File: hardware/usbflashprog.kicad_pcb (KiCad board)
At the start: 2 copper layers, 211 x 122 mm, 123 parts, among them J1 12-18V, J2 Parallel Adapter, J3 Serial Adapter, Q1 BC547, Q10 BC557, Q11 BC557, Q12 BC547, Q13 BC547, Q14 BC547, Q15 BC547, Q16 BC547, Q2 BC327, Q3 BC327, Q4 BC327, Q5 TIP120, Q6 BC327, Q7 BC557, Q8 BC557, Q9 BC557, U1 7809, U10 74HC595, U11 74HC165, U12 74HC165, U2 74LS06N, U3 Pico, U4 74HC595, U5 74HC595, U6 74HC595, U7 74HC595, U8 74LS06N, U9 74HC595

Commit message: Rev.E. Updated specifications document and hardware design.
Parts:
- C1, C2, C6: footprint Capacitor_THT:CP_Radial_D8.0mm_P3.50mm -> Capacitor_THT:CP_Radial_D5.0mm_P2.50mm
- C4: footprint Capacitor_THT:CP_Radial_D10.0mm_P7.50mm -> Capacitor_THT:CP_Radial_D8.0mm_P3.80mm
- C8: footprint Capacitor_THT:C_Disc_D6.0mm_W2.5mm_P5.00mm -> Capacitor_THT:CP_Radial_D8.0mm_P3.50mm
- L2: footprint Inductor_THT:L_Toroid_Vertical_L16.0mm_W8.0mm_P7.62mm -> Inductor_THT:L_Toroid_Vertical_L13.0mm_W6.5mm_P5.60mm
- R52: footprint Resistor_THT:R_Axial_DIN0207_L6.3mm_D2.5mm_P10.16mm_Horizontal -> Resistor_THT:R_Axial_DIN0309_L9.0mm_D3.2mm_P15.24mm_Horizontal
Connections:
- net /Control Signals/~{OEINT} renamed Net-(D14-Pad2)
- net /Control Signals/~{WEINT} renamed Net-(D15-Pad2)

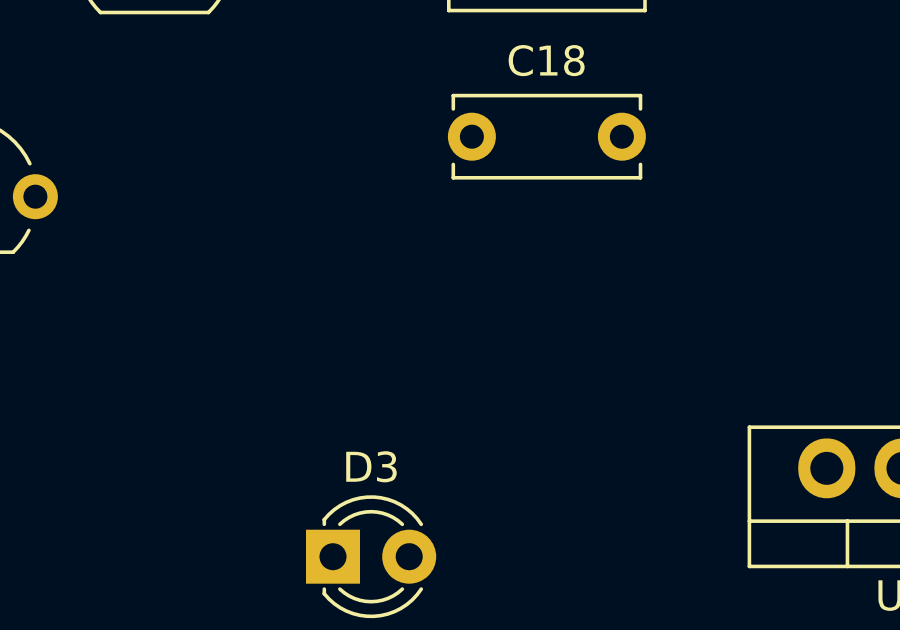
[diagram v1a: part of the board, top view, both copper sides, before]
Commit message: Rev.E. Add Test Points for VDD/VPP/GND.
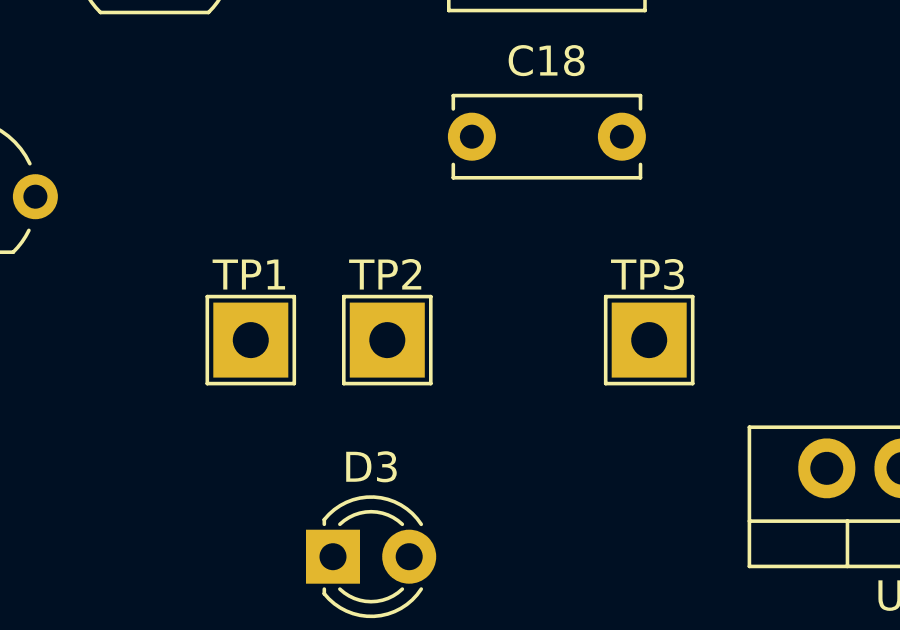
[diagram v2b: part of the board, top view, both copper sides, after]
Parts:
- added TP1: VDD, TestPoint:TestPoint_THTPad_2.5x2.5mm_Drill1.2mm, F.Cu at (175.3, 144.8)
- added TP2: GND, TestPoint:TestPoint_THTPad_2.5x2.5mm_Drill1.2mm, F.Cu at (179.8, 144.8)
- added TP3: VPP, TestPoint:TestPoint_THTPad_2.5x2.5mm_Drill1.2mm, F.Cu at (188.5, 144.8)

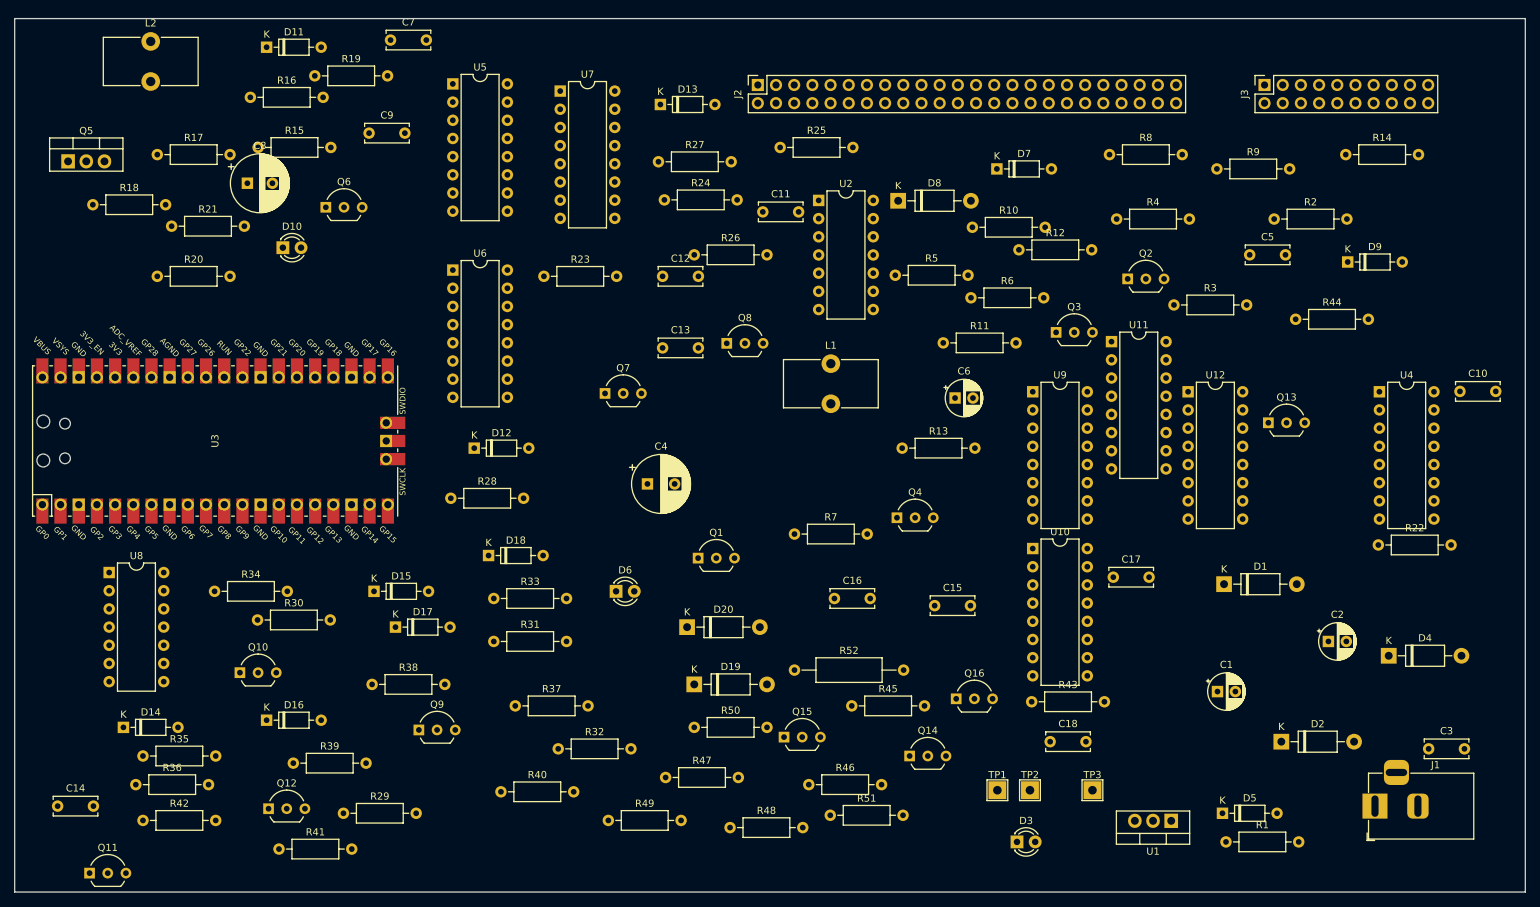
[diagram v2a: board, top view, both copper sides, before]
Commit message: Rev.G. Change external power supply to a MT3606 DC-DC Module
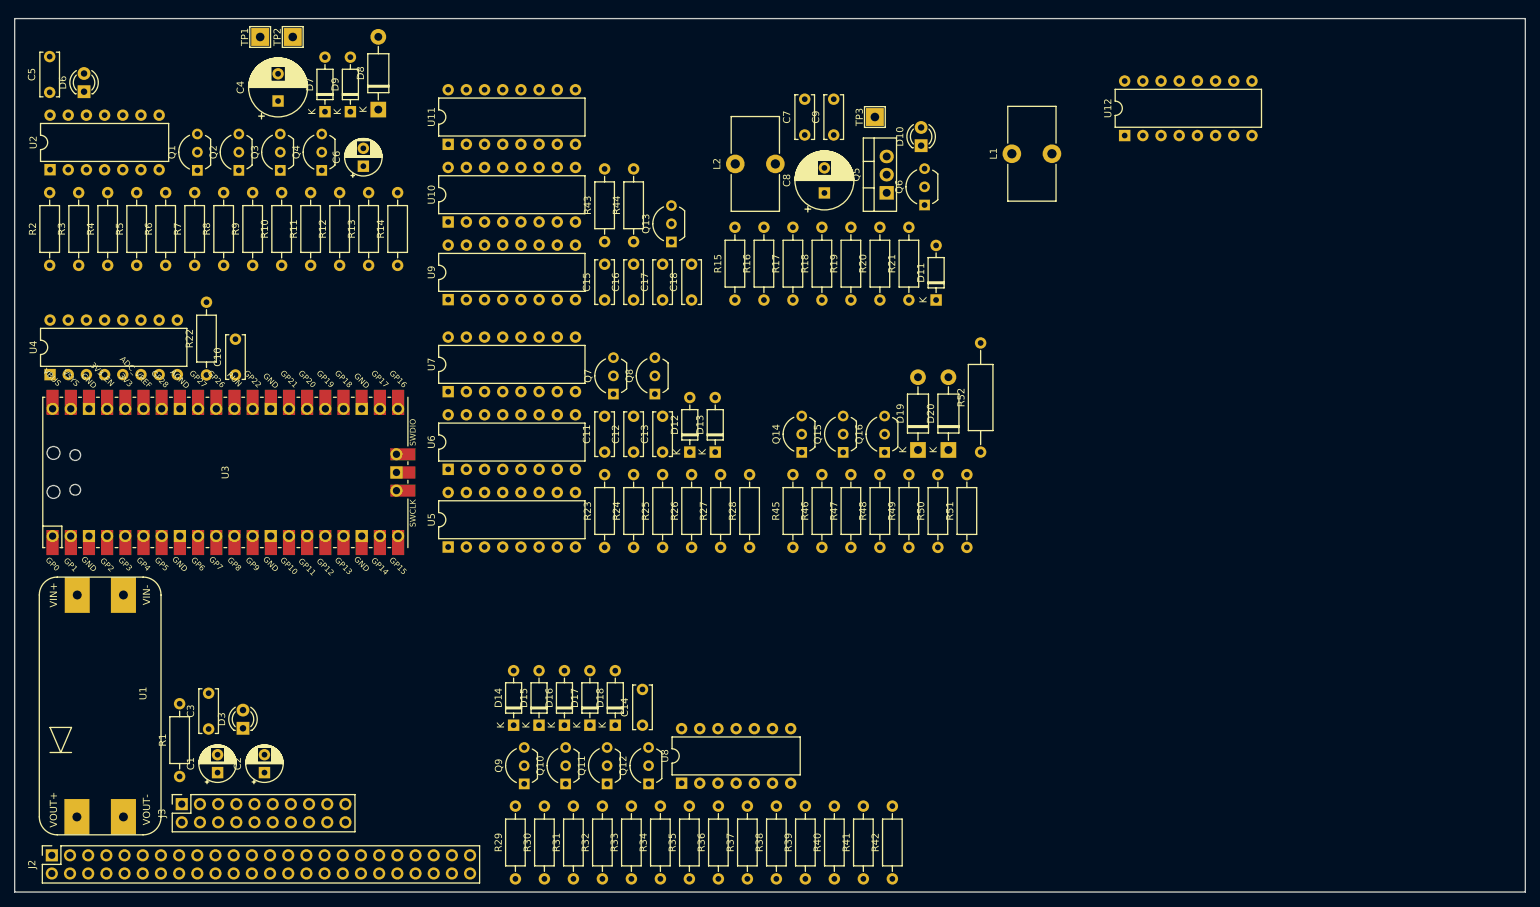
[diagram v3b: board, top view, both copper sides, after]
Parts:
- removed D1, D2, D4: 1N4001, Diode_THT:D_DO-41_SOD81_P10.16mm_Horizontal
- removed D5: BAT46, Diode_THT:D_DO-35_SOD27_P7.62mm_Horizontal
- removed J1: 12-18V, Connector_BarrelJack:BarrelJack_Horizontal
- U1: value 7809 -> MT3608 Module; footprint Package_TO_SOT_THT:TO-220-3_Vertical -> DC2DC_Modules:MT3608_module
- moved U4 185.7 mm to (42.9, 86.7), turned to 90 degrees
- moved J3 181.6 mm to (61.3, 146.7)
- moved R2 171.2 mm to (42.9, 71.5), turned to 90 degrees
- moved C10 171.0 mm to (68.8, 86.8), turned to 90 degrees
- moved C3 170.4 mm to (65.1, 136.2), turned to 90 degrees
- moved C5 169.1 mm to (42.9, 47.3), turned to 90 degrees
- moved R22 165.4 mm to (64.8, 86.8), turned to 90 degrees
- moved R3 153.1 mm to (46.9, 71.5), turned to 90 degrees
- moved U1 150.6 mm to (49.9, 131.5), turned to 90 degrees
- moved C2 149.7 mm to (72.9, 142.3), turned to 90 degrees
- moved TP1 147.2 mm to (72.3, 39.6), turned to 90 degrees
- moved TP2 147.2 mm to (76.8, 39.6), turned to 90 degrees
- moved R1 146.4 mm to (61.0, 142.9), turned to 90 degrees
- moved J2 145.9 mm to (43.2, 153.9)
- moved R4 141.1 mm to (51.0, 71.5), turned to 90 degrees
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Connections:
- C1 pad 1: Net-(C1-Pad1) -> +5V
- Q11 pad 1: Net-(Q11-Pad1) -> Net-(Q11-C)
- R1 pad 1: Net-(D4-Pad2) -> +9V
- R40 pad 1: Net-(Q11-Pad1) -> /~{CE}
- R40 pad 2: /~{CE} -> Net-(Q11-C)
- U1 pad 1: Net-(C1-Pad1) -> +5V
- U1 pad 2: Net-(D2-Pad2) -> GND
- U1 pad 3: Net-(D4-Pad2) -> GND
